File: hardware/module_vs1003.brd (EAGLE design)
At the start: 109.9 x 68.6 mm, 119 parts, among them IC1 IC_USBLC6-2, IC2 LM1117IMPX-3.3, IC3 PIC32MX795F512, IC4 DP83848, IC5 LM1117MPX-2.5, U1 USD-SOCKETUSD, U2 VS1003, X2 CRYSTALS-NOGND-CFPX-217, X3 KUSBVX, Y3 CRYSTAL-GROUNDEDSMD-5X3.2

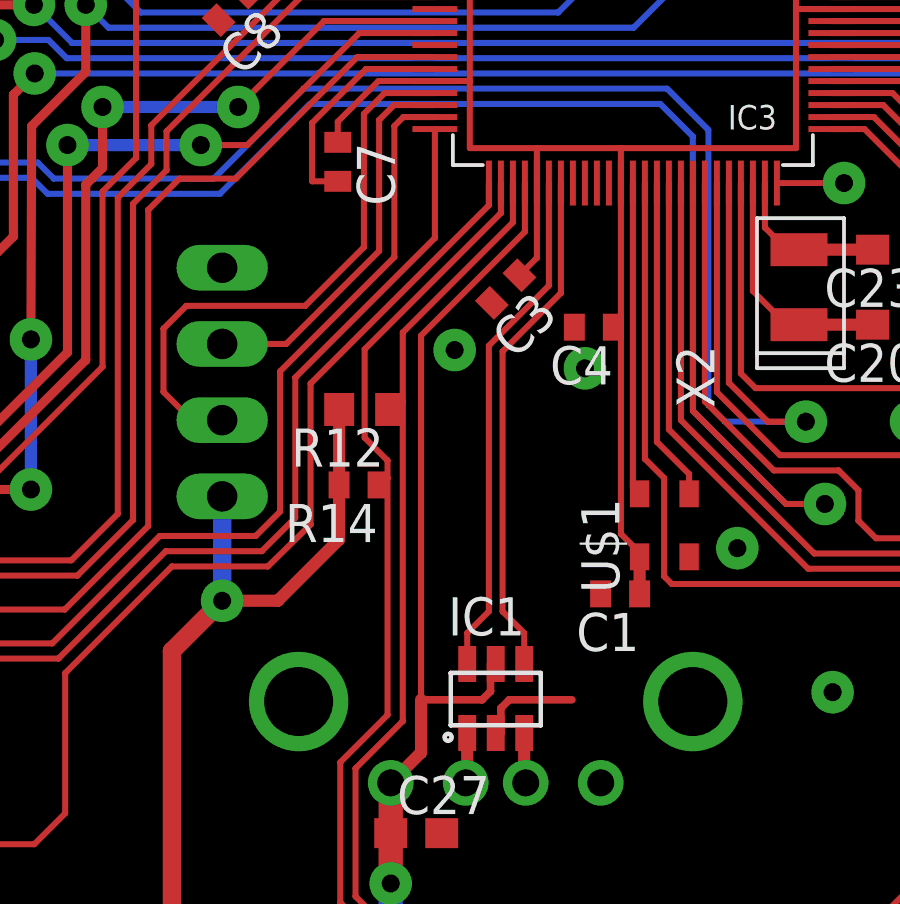
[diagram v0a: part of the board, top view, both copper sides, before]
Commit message: Changes in PCB design allowing us to use bug free I2C1 instead of buggy I2C3
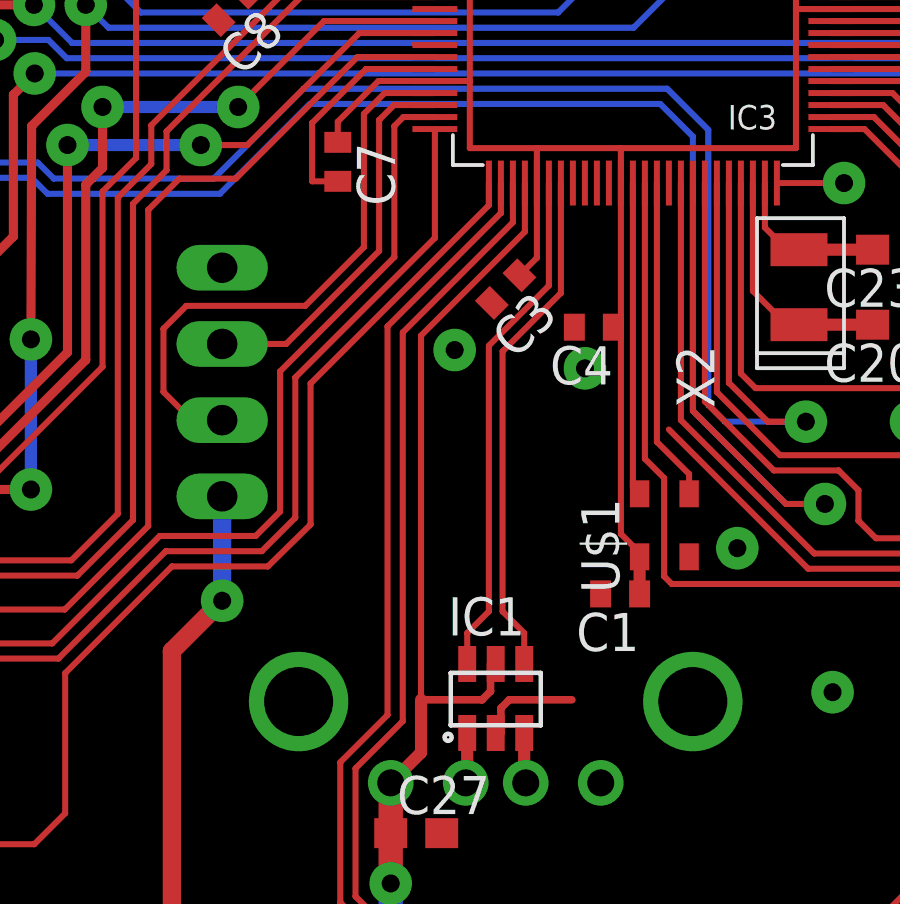
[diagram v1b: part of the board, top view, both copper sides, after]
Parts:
- removed R12: (no value), rcl:R0603
- removed R14: (no value), rcl:R0402
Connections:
- net 1WIRE renamed SCL1
- net RA15_ROT_SW renamed SDA1
- removed net SCL1A: IC3.53, R12.1, SV1.1
- removed net SDA1A: IC3.52, R14.1, SV1.2
- new net RF2_ROT_SW: IC3.52, SV1.2
- new net RF8: IC3.53, SV1.1
- net 3V: no longer R12.2, R14.2
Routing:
- net SCL1A: track 49.0 -> 0.00 mm
- net SDA1A: track 48.4 -> 0.00 mm
- net RF8: track 0.00 -> 48.4 mm
- net RF2_ROT_SW: track 0.00 -> 47.4 mm
- net 3V: track 526.5 -> 517.4 mm
- net SCL1: track 28.2 -> 20.0 mm
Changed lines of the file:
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@@
 <?xml version="1.0" encoding="utf-8"?>
 <!DOCTYPE eagle SYSTEM "eagle.dtd">
-<eagle version="7.7.0">
+<eagle version="7.2.0">
 <drawing>
 <settings>
@@
 </element>
 <element name="C1" library="rcl" package="C0402" value="" x="49.86601875" y="18.9992" rot="R180"/>
-<element name="R12" library="rcl" package="R0603" value="" x="41.3512" y="25.146" rot="R180"/>
-<element name="R14" library="rcl" package="R0402" value="" x="41.148" y="22.6314" rot="R180"/>
 <element name="C2" library="rcl" package="C0402" value="" x="26.126440625" y="25.5016"/>
 <element name="L3" library="dp_devices" package="FB805" value="" x="11.938" y="38.4302" rot="MR180"/>
@@
 <wire x1="43.692" y1="39.6938" x2="38.0555" y2="39.6938" width="0.2032" layer="1"/>
 <wire x1="38.0555" y1="39.6938" x2="37.40391875" y2="39.04221875" width="0.2032" layer="1"/>
-<contactref element="R12" pad="2"/>
-<contactref element="R14" pad="2"/>
-<wire x1="40.5012" y1="25.146" x2="40.5012" y2="22.6346" width="0.4064" layer="1"/>
-<wire x1="40.5012" y1="22.6346" x2="40.498" y2="22.6314" width="0.4064" layer="1"/>
-<wire x1="40.498" y1="22.6314" x2="40.498" y2="20.813" width="0.4064" layer="1"/>
-<wire x1="36.6014" y1="18.7706" x2="38.4556" y2="18.7706" width="0.4064" layer="1"/>
-<wire x1="38.4556" y1="18.7706" x2="40.498" y2="20.813" width="0.4064" layer="1"/>
 <wire x1="36.6014" y1="18.7706" x2="36.6014" y2="22.2504" width="0.6096" layer="16"/>
 <wire x1="36.6014" y1="18.7706" x2="34.925" y2="17.0942" width="0.6096" layer="1"/>
@@
 <wire x1="63.373" y1="14.351" x2="65.659" y2="12.065" width="0.2032" layer="1"/>
 </signal>
-<signal name="1WIRE">
-<contactref element="IC3" pad="66"/>
-<wire x1="51.492" y1="32.6938" x2="51.492" y2="24.4794" width="0.2032" layer="1"/>
-<contactref element="SV1" pad="3"/>
-<wire x1="51.492" y1="24.4794" x2="56.134" y2="19.8374" width="0.2032" layer="1"/>
-<wire x1="56.134" y1="19.8374" x2="60.833" y2="19.8374" width="0.2032" layer="1"/>
-<wire x1="60.833" y1="19.8374" x2="62.357" y2="18.3134" width="0.2032" layer="1"/>
-<wire x1="62.357" y1="18.3134" x2="62.357" y2="12.827" width="0.2032" layer="1"/>
-<wire x1="62.357" y1="12.827" x2="63.119" y2="12.065" width="0.2032" layer="1"/>
-</signal>
 <signal name="AN_3V">
 <contactref element="IC3" pad="30"/>
@@
 <wire x1="28.702" y1="63.0682" x2="30.2768" y2="64.643" width="0.4064" layer="1"/>
 </signal>
-<signal name="SCL1A">
-<contactref element="IC3" pad="53"/>
-<wire x1="46.292" y1="32.6938" x2="46.292" y2="31.3822" width="0.2032" layer="1"/>
-<wire x1="42.6212" y1="27.7114" x2="46.292" y2="31.3822" width="0.2032" layer="1"/>
-<contactref element="SV1" pad="1"/>
-<wire x1="42.6212" y1="14.7574" x2="41.0464" y2="13.1826" width="0.2032" layer="1"/>
-<wire x1="41.0464" y1="13.1826" x2="41.0464" y2="8.9154" width="0.2032" layer="1"/>
-<wire x1="41.0464" y1="8.9154" x2="41.7322" y2="8.2296" width="0.2032" layer="1"/>
-<wire x1="41.7322" y1="8.2296" x2="58.5724" y2="8.2296" width="0.2032" layer="1"/>
-<wire x1="58.5724" y1="8.2296" x2="59.3344" y2="8.9916" width="0.2032" layer="1"/>
-<wire x1="59.3344" y1="8.9916" x2="59.3344" y2="10.8204" width="0.2032" layer="1"/>
-<wire x1="59.3344" y1="10.8204" x2="60.579" y2="12.065" width="0.2032" layer="1"/>
-<contactref element="R12" pad="1"/>
-<wire x1="42.6212" y1="27.7114" x2="42.6212" y2="25.4" width="0.2032" layer="1"/>
-<wire x1="42.6212" y1="25.4" x2="42.6212" y2="14.7574" width="0.2032" layer="1"/>
-<wire x1="42.2012" y1="25.146" x2="42.3672" y2="25.146" width="0.2032" layer="1"/>
-<wire x1="42.3672" y1="25.146" x2="42.6212" y2="25.4" width="0.2032" layer="1"/>
-</signal>
 <signal name="DP_RST">
 <contactref element="R1" pad="2"/>
@@
 <wire x1="61.849" y1="10.795" x2="63.119" y2="9.525" width="0.2032" layer="1"/>
 </signal>
-<signal name="SDA1A">
+<signal name="SCL1">
+<contactref element="IC3" pad="66"/>
+<contactref element="SV1" pad="3"/>
+<wire x1="51.492" y1="24.4794" x2="56.134" y2="19.8374" width="0.2032" layer="1"/>
+<wire x1="56.134" y1="19.8374" x2="60.833" y2="19.8374" width="0.2032" layer="1"/>
+<wire x1="60.833" y1="19.8374" x2="62.357" y2="18.3134" width="0.2032" layer="1"/>
+<wire x1="62.357" y1="18.3134" x2="62.357" y2="12.827" width="0.2032" layer="1"/>
+<wire x1="62.357" y1="12.827" x2="63.119" y2="12.065" width="0.2032" layer="1"/>
+<wire x1="51.492" y1="24.4794" x2="51.492" y2="32.6938" width="0" layer="19" extent="1-1"/>
+</signal>
+<signal name="RF2_ROT_SW">
 <contactref element="IC3" pad="52"/>
-<wire x1="45.892" y1="32.6938" x2="45.892" y2="31.6934" width="0.2032" layer="1"/>
-<wire x1="45.892" y1="31.6934" x2="41.3512" y2="27.1526" width="0.2032" layer="1"/>
+<wire x1="45.892" y1="31.6934" x2="42.1132" y2="27.9146" width="0.2032" layer="1"/>
 <contactref element="SV1" pad="2"/>
 <wire x1="40.5384" y1="13.3858" x2="40.5384" y2="8.7122" width="0.2032" layer="1"/>
@@
 <wire x1="41.529" y1="7.7216" x2="58.7756" y2="7.7216" width="0.2032" layer="1"/>
 <wire x1="58.7756" y1="7.7216" x2="60.579" y2="9.525" width="0.2032" layer="1"/>
-<contactref element="R14" pad="1"/>
 <wire x1="42.1132" y1="14.9606" x2="40.5384" y2="13.3858" width="0.2032" layer="1"/>
-<wire x1="41.3512" y1="27.1526" x2="41.3512" y2="24.2062" width="0.2032" layer="1"/>
-<wire x1="42.1132" y1="23.4442" x2="42.1132" y2="22.86" width="0.2032" layer="1"/>
-<wire x1="42.1132" y1="22.86" x2="42.1132" y2="14.9606" width="0.2032" layer="1"/>
-<wire x1="41.798" y1="22.6314" x2="41.8846" y2="22.6314" width="0.2032" layer="1"/>
-<wire x1="41.8846" y1="22.6314" x2="42.1132" y2="22.86" width="0.2032" layer="1"/>
-<wire x1="41.3512" y1="24.2062" x2="42.1132" y2="23.4442" width="0.2032" layer="1"/>
-</signal>
-<signal name="RA15_ROT_SW">
+<wire x1="42.1132" y1="27.9146" x2="42.1132" y2="14.9606" width="0.2032" layer="1"/>
+<wire x1="45.892" y1="31.6934" x2="45.892" y2="32.6938" width="0.2032" layer="1"/>
+</signal>
+<signal name="RF8">
+<contactref element="IC3" pad="53"/>
+<wire x1="42.6212" y1="27.7114" x2="46.292" y2="31.3822" width="0.2032" layer="1"/>
+<contactref element="SV1" pad="1"/>
+<wire x1="42.6212" y1="14.7574" x2="41.0464" y2="13.1826" width="0.2032" layer="1"/>
+<wire x1="41.0464" y1="13.1826" x2="41.0464" y2="8.9154" width="0.2032" layer="1"/>
+<wire x1="41.0464" y1="8.9154" x2="41.7322" y2="8.2296" width="0.2032" layer="1"/>
+<wire x1="41.7322" y1="8.2296" x2="58.5724" y2="8.2296" width="0.2032" layer="1"/>
+<wire x1="58.5724" y1="8.2296" x2="59.3344" y2="8.9916" width="0.2032" layer="1"/>
+<wire x1="59.3344" y1="8.9916" x2="59.3344" y2="10.8204" width="0.2032" layer="1"/>
+<wire x1="59.3344" y1="10.8204" x2="60.579" y2="12.065" width="0.2032" layer="1"/>
+<wire x1="42.6212" y1="27.7114" x2="42.6212" y2="14.7574" width="0.2032" layer="1"/>
+<wire x1="46.292" y1="31.3822" x2="46.292" y2="32.6938" width="0.2032" layer="1"/>
+</signal>
+<signal name="SDA1">
 <contactref element="IC3" pad="67"/>
 <wire x1="51.892" y1="24.7906" x2="56.3372" y2="20.3454" width="0.2032" layer="1"/>
@@
 <wire x1="64.389" y1="12.5984" x2="64.389" y2="10.795" width="0.2032" layer="1"/>
 <wire x1="64.389" y1="10.795" x2="65.659" y2="9.525" width="0.2032" layer="1"/>
-<wire x1="51.892" y1="32.6938" x2="51.892" y2="24.7906" width="0.2032" layer="1"/>
+<wire x1="51.892" y1="24.7906" x2="51.892" y2="32.6938" width="0.2032" layer="1"/>
 </signal>
 </signals>
